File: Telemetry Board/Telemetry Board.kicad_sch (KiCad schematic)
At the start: 12 parts, among them J1 776180-1, U3 CD74HC4067SM96, U4 ISO1050DUB, U5 NUCLEO-L432KC

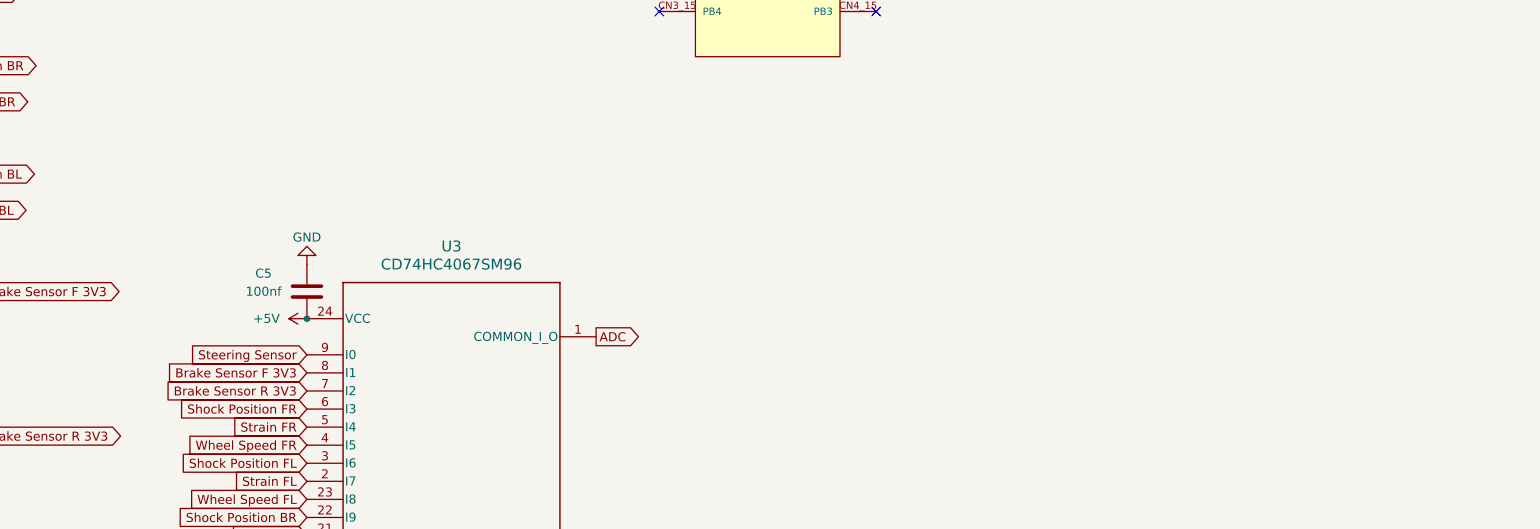
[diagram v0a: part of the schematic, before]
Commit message: Telemetry Board V1
Also tiny BSPD silk screen change (L432KC instead of LM432KC)
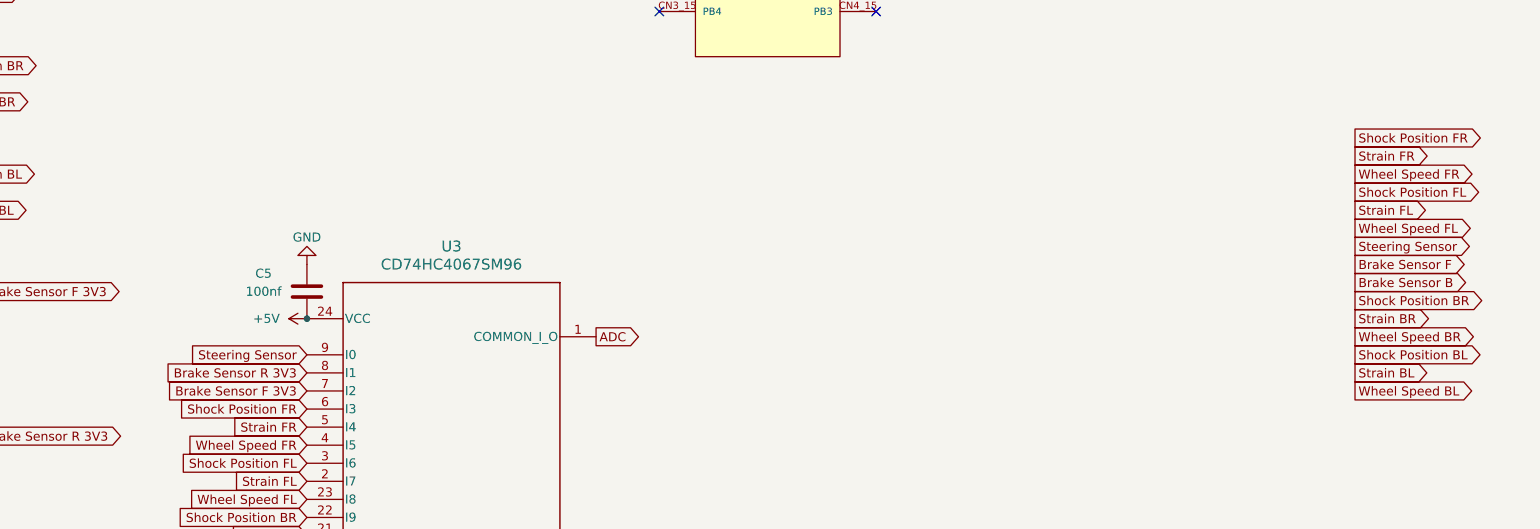
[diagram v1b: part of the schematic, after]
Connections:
- net Brake Sensor F 3V3: now also U3.7 (I2); no longer U3.8 (I1)
- net Brake Sensor R 3V3: now also U3.8 (I1); no longer U3.7 (I2)
